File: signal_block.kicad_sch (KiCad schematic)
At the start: 9 parts, among them J6 Conn_01x04

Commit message: 24V Regulator, Pyro Igniter Circuit
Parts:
- renumbered J6 to J4
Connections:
- net SIGNAL_P: now reaches J4.2 (Pin_2), R14.2, R16.1, TC1.1 (+)
- net SIGNAL_N: now reaches J4.3 (Pin_3), R15.1, R17.1, TC1.2 (-)
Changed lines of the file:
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@@
+		)
+	)
+	(label "SIGNAL_N"
+		(at 125.73 93.98 0)
+		(effects
+			(font
+				(size 1.27 1.27)
+			)
+			(justify left bottom)
+		)
+	)
+	(label "SIGNAL_P"
+		(at 125.73 91.44 0)
+		(effects
+			(font
+				(size 1.27 1.27)
+			)
+			(justify left bottom)
 		)
 	)
@@
 		(in_pos_files yes)
 		(dnp no)
-		(property "Reference" "J6"
+		(property "Reference" "J4"
 			(at 116.84 83.058 0)
 			(show_name no)
@@
 			(project "mixed_signal_sensor_board"
 				(path "/5c142d60-6b5a-463f-88b9-a177eae7f51b/26b48b96-d6f0-4640-a594-6ae05ce5f71b"
+					(reference "J4")
+					(unit 1)
+				)
+				(path "/5c142d60-6b5a-463f-88b9-a177eae7f51b/3d2fab60-312f-4afa-9448-ea43b3519a6a"
+					(reference "J9")
+					(unit 1)
+				)
+				(path "/5c142d60-6b5a-463f-88b9-a177eae7f51b/83995c98-2fb2-4e6b-8c1a-49363bfa6bab"
+					(reference "J5")
+					(unit 1)
+				)
+				(path "/5c142d60-6b5a-463f-88b9-a177eae7f51b/8e376074-b16c-4624-98ef-c910278a89e5"
 					(reference "J6")
 					(unit 1)
 				)
-				(path "/5c142d60-6b5a-463f-88b9-a177eae7f51b/3d2fab60-312f-4afa-9448-ea43b3519a6a"
+				(path "/5c142d60-6b5a-463f-88b9-a177eae7f51b/a20a6c68-f4f4-4b40-90d6-d2c7554cb778"
 					(reference "J11")
 					(unit 1)
 				)
-				(path "/5c142d60-6b5a-463f-88b9-a177eae7f51b/83995c98-2fb2-4e6b-8c1a-49363bfa6bab"
+				(path "/5c142d60-6b5a-463f-88b9-a177eae7f51b/b2385cce-9f51-4d63-9d92-5a2772ad4011"
 					(reference "J7")
 					(unit 1)
 				)
-				(path "/5c142d60-6b5a-463f-88b9-a177eae7f51b/8e376074-b16c-4624-98ef-c910278a89e5"
+				(path "/5c142d60-6b5a-463f-88b9-a177eae7f51b/c788519d-2f00-4572-8a46-36c8c3e2499e"
 					(reference "J8")
 					(unit 1)
 				)
-				(path "/5c142d60-6b5a-463f-88b9-a177eae7f51b/a20a6c68-f4f4-4b40-90d6-d2c7554cb778"
-					(reference "J13")
-					(unit 1)
-				)
-				(path "/5c142d60-6b5a-463f-88b9-a177eae7f51b/b2385cce-9f51-4d63-9d92-5a2772ad4011"
-					(reference "J9")
-					(unit 1)
-				)
-				(path "/5c142d60-6b5a-463f-88b9-a177eae7f51b/c788519d-2f00-4572-8a46-36c8c3e2499e"
+				(path "/5c142d60-6b5a-463f-88b9-a177eae7f51b/fe701933-2939-43ec-a76b-ec9b5f6332a0"
 					(reference "J10")
-					(unit 1)
-				)
-				(path "/5c142d60-6b5a-463f-88b9-a177eae7f51b/fe701933-2939-43ec-a76b-ec9b5f6332a0"
-					(reference "J12")
 					(unit 1)
 				)
@@
 		(dnp no)
 		(fields_autoplaced yes)
-		(property "Reference" "#PWR059"
+		(property "Reference" "#PWR055"
 			(at 151.13 81.28 0)
 			(hide yes)
@@
 			(project "mixed_signal_sensor_board"
 				(path "/5c142d60-6b5a-463f-88b9-a177eae7f51b/26b48b96-d6f0-4640-a594-6ae05ce5f71b"
-					(reference "#PWR059")
+					(reference "#PWR055")
 					(unit 1)
 				)
 				(path "/5c142d60-6b5a-463f-88b9-a177eae7f51b/3d2fab60-312f-4afa-9448-ea43b3519a6a"
-					(reference "#PWR084")
+					(reference "#PWR080")
 					(unit 1)
 				)
 				(path "/5c142d60-6b5a-463f-88b9-a177eae7f51b/83995c98-2fb2-4e6b-8c1a-49363bfa6bab"
-					(reference "#PWR064")
+					(reference "#PWR060")
 					(unit 1)
 				)
 				(path "/5c142d60-6b5a-463f-88b9-a177eae7f51b/8e376074-b16c-4624-98ef-c910278a89e5"
-					(reference "#PWR069")
+					(reference "#PWR065")
 					(unit 1)
 				)
 				(path "/5c142d60-6b5a-463f-88b9-a177eae7f51b/a20a6c68-f4f4-4b40-90d6-d2c7554cb778"
-					(reference "#PWR094")
+					(reference "#PWR090")
 					(unit 1)
 				)
 				(path "/5c142d60-6b5a-463f-88b9-a177eae7f51b/b2385cce-9f51-4d63-9d92-5a2772ad4011"
-					(reference "#PWR074")
+					(reference "#PWR070")
 					(unit 1)
 				)
 				(path "/5c142d60-6b5a-463f-88b9-a177eae7f51b/c788519d-2f00-4572-8a46-36c8c3e2499e"
-					(reference "#PWR079")
+					(reference "#PWR075")
 					(unit 1)
 				)
 				(path "/5c142d60-6b5a-463f-88b9-a177eae7f51b/fe701933-2939-43ec-a76b-ec9b5f6332a0"
-					(reference "#PWR089")
+					(reference "#PWR085")
 					(unit 1)
 				)
@@
 		(dnp no)
 		(fields_autoplaced yes)
-		(property "Reference" "#PWR058"
+		(property "Reference" "#PWR054"
 			(at 120.65 96.52 0)
 			(hide yes)
@@
 			(project "mixed_signal_sensor_board"
 				(path "/5c142d60-6b5a-463f-88b9-a177eae7f51b/26b48b96-d6f0-4640-a594-6ae05ce5f71b"
-					(reference "#PWR058")
+					(reference "#PWR054")
 					(unit 1)
 				)
 				(path "/5c142d60-6b5a-463f-88b9-a177eae7f51b/3d2fab60-312f-4afa-9448-ea43b3519a6a"
-					(reference "#PWR083")
+					(reference "#PWR079")
 					(unit 1)
 				)
 				(path "/5c142d60-6b5a-463f-88b9-a177eae7f51b/83995c98-2fb2-4e6b-8c1a-49363bfa6bab"
-					(reference "#PWR063")
+					(reference "#PWR059")
 					(unit 1)
 				)
 				(path "/5c142d60-6b5a-463f-88b9-a177eae7f51b/8e376074-b16c-4624-98ef-c910278a89e5"
-					(reference "#PWR068")
+					(reference "#PWR064")
 					(unit 1)
 				)
 				(path "/5c142d60-6b5a-463f-88b9-a177eae7f51b/a20a6c68-f4f4-4b40-90d6-d2c7554cb778"
-					(reference "#PWR093")
+					(reference "#PWR089")
 					(unit 1)
 				)
 				(path "/5c142d60-6b5a-463f-88b9-a177eae7f51b/b2385cce-9f51-4d63-9d92-5a2772ad4011"
-					(reference "#PWR073")
+					(reference "#PWR069")
 					(unit 1)
 				)
 				(path "/5c142d60-6b5a-463f-88b9-a177eae7f51b/c788519d-2f00-4572-8a46-36c8c3e2499e"
-					(reference "#PWR078")
+					(reference "#PWR074")
 					(unit 1)
 				)
 				(path "/5c142d60-6b5a-463f-88b9-a177eae7f51b/fe701933-2939-43ec-a76b-ec9b5f6332a0"
-					(reference "#PWR088")
+					(reference "#PWR084")
 					(unit 1)
 				)
@@
 		(dnp no)
 		(fields_autoplaced yes)
-		(property "Reference" "#PWR060"
+		(property "Reference" "#PWR056"
 			(at 151.13 114.3 0)
 			(hide yes)
@@
 			(project "mixed_signal_sensor_board"
 				(path "/5c142d60-6b5a-463f-88b9-a177eae7f51b/26b48b96-d6f0-4640-a594-6ae05ce5f71b"
-					(reference "#PWR060")
+					(reference "#PWR056")
 					(unit 1)
 				)
 				(path "/5c142d60-6b5a-463f-88b9-a177eae7f51b/3d2fab60-312f-4afa-9448-ea43b3519a6a"
-					(reference "#PWR085")
+					(reference "#PWR081")
 					(unit 1)
 				)
 				(path "/5c142d60-6b5a-463f-88b9-a177eae7f51b/83995c98-2fb2-4e6b-8c1a-49363bfa6bab"
-					(reference "#PWR065")
+					(reference "#PWR061")
 					(unit 1)
 				)
 				(path "/5c142d60-6b5a-463f-88b9-a177eae7f51b/8e376074-b16c-4624-98ef-c910278a89e5"
-					(reference "#PWR070")
+					(reference "#PWR066")
 					(unit 1)
 				)
 				(path "/5c142d60-6b5a-463f-88b9-a177eae7f51b/a20a6c68-f4f4-4b40-90d6-d2c7554cb778"
-					(reference "#PWR095")
+					(reference "#PWR091")
 					(unit 1)
 				)
 				(path "/5c142d60-6b5a-463f-88b9-a177eae7f51b/b2385cce-9f51-4d63-9d92-5a2772ad4011"
-					(reference "#PWR075")
+					(reference "#PWR071")
 					(unit 1)
 				)
 				(path "/5c142d60-6b5a-463f-88b9-a177eae7f51b/c788519d-2f00-4572-8a46-36c8c3e2499e"
-					(reference "#PWR080")
+					(reference "#PWR076")
 					(unit 1)
 				)
 				(path "/5c142d60-6b5a-463f-88b9-a177eae7f51b/fe701933-2939-43ec-a76b-ec9b5f6332a0"
-					(reference "#PWR090")
+					(reference "#PWR086")
 					(unit 1)
 				)
@@
 		(dnp no)
 		(fields_autoplaced yes)
-		(property "Reference" "#PWR057"
+		(property "Reference" "#PWR053"
 			(at 120.65 88.9 0)
 			(hide yes)
@@
 			(project "mixed_signal_sensor_board"
 				(path "/5c142d60-6b5a-463f-88b9-a177eae7f51b/26b48b96-d6f0-4640-a594-6ae05ce5f71b"
-					(reference "#PWR057")
+					(reference "#PWR053")
 					(unit 1)
 				)
 				(path "/5c142d60-6b5a-463f-88b9-a177eae7f51b/3d2fab60-312f-4afa-9448-ea43b3519a6a"
-					(reference "#PWR082")
+					(reference "#PWR078")
 					(unit 1)
 				)
 				(path "/5c142d60-6b5a-463f-88b9-a177eae7f51b/83995c98-2fb2-4e6b-8c1a-49363bfa6bab"
-					(reference "#PWR062")
+					(reference "#PWR058")
 					(unit 1)
 				)
 				(path "/5c142d60-6b5a-463f-88b9-a177eae7f51b/8e376074-b16c-4624-98ef-c910278a89e5"
-					(reference "#PWR067")
+					(reference "#PWR063")
 					(unit 1)
 				)
 				(path "/5c142d60-6b5a-463f-88b9-a177eae7f51b/a20a6c68-f4f4-4b40-90d6-d2c7554cb778"
-					(reference "#PWR092")
+					(reference "#PWR088")
 					(unit 1)
 				)
 				(path "/5c142d60-6b5a-463f-88b9-a177eae7f51b/b2385cce-9f51-4d63-9d92-5a2772ad4011"
-					(reference "#PWR072")
+					(reference "#PWR068")
 					(unit 1)
 				)
 				(path "/5c142d60-6b5a-463f-88b9-a177eae7f51b/c788519d-2f00-4572-8a46-36c8c3e2499e"
-					(reference "#PWR077")
+					(reference "#PWR073")
 					(unit 1)
 				)
 				(path "/5c142d60-6b5a-463f-88b9-a177eae7f51b/fe701933-2939-43ec-a76b-ec9b5f6332a0"
-					(reference "#PWR087")
+					(reference "#PWR083")
 					(unit 1)
 				)
@@
 		(dnp no)
 		(fields_autoplaced yes)
-		(property "Reference" "#PWR061"
+		(property "Reference" "#PWR057"
 			(at 193.04 92.71 0)
 			(hide yes)
@@
 			(project "mixed_signal_sensor_board"
 				(path "/5c142d60-6b5a-463f-88b9-a177eae7f51b/26b48b96-d6f0-4640-a594-6ae05ce5f71b"
-					(reference "#PWR061")
+					(reference "#PWR057")
 					(unit 1)
 				)
 				(path "/5c142d60-6b5a-463f-88b9-a177eae7f51b/3d2fab60-312f-4afa-9448-ea43b3519a6a"
-					(reference "#PWR086")
+					(reference "#PWR082")
 					(unit 1)
 				)
 				(path "/5c142d60-6b5a-463f-88b9-a177eae7f51b/83995c98-2fb2-4e6b-8c1a-49363bfa6bab"
-					(reference "#PWR066")
+					(reference "#PWR062")
 					(unit 1)
 				)
 				(path "/5c142d60-6b5a-463f-88b9-a177eae7f51b/8e376074-b16c-4624-98ef-c910278a89e5"
-					(reference "#PWR071")
+					(reference "#PWR067")
 					(unit 1)
 				)
 				(path "/5c142d60-6b5a-463f-88b9-a177eae7f51b/a20a6c68-f4f4-4b40-90d6-d2c7554cb778"
-					(reference "#PWR096")
+					(reference "#PWR092")
 					(unit 1)
 				)
 				(path "/5c142d60-6b5a-463f-88b9-a177eae7f51b/b2385cce-9f51-4d63-9d92-5a2772ad4011"
-					(reference "#PWR076")
+					(reference "#PWR072")
 					(unit 1)
 				)
 				(path "/5c142d60-6b5a-463f-88b9-a177eae7f51b/c788519d-2f00-4572-8a46-36c8c3e2499e"
-					(reference "#PWR081")
+					(reference "#PWR077")
 					(unit 1)
 				)
 				(path "/5c142d60-6b5a-463f-88b9-a177eae7f51b/fe701933-2939-43ec-a76b-ec9b5f6332a0"
-					(reference "#PWR091")
-					(unit 1)
-				)
+					(reference "#PWR087")
+					(unit 1)
+				)

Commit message: Pyro fault detection, Decoupling Caps STM32, Initial PCB Layout
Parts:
- renumbered C23 to C29, C24 to C30, C25 to C31
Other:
- moved on the sheet: C29, C30, C31, J4, R14, R15, R16, R17, TC1

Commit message: Step files, SMD connectors, reduced size
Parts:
- J4: footprint Connector_JST:JST_XH_S4B-XH-A_1x04_P2.50mm_Horizontal -> Connector_JST:JST_PH_S4B-PH-SM4-TB_1x04-1MP_P2.00mm_Horizontal
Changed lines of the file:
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@@
 			)
 		)
-		(property "Footprint" "Connector_JST:JST_XH_S4B-XH-A_1x04_P2.50mm_Horizontal"
+		(property "Footprint" "Connector_JST:JST_PH_S4B-PH-SM4-TB_1x04-1MP_P2.00mm_Horizontal"
 			(at 110.49 97.79 0)
 			(hide yes)

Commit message: replaced signal blocks, shortening board, adding precise positioning
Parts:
- renumbered J4 to J5, R14 to R15, R15 to R16, R16 to R17, R17 to R18

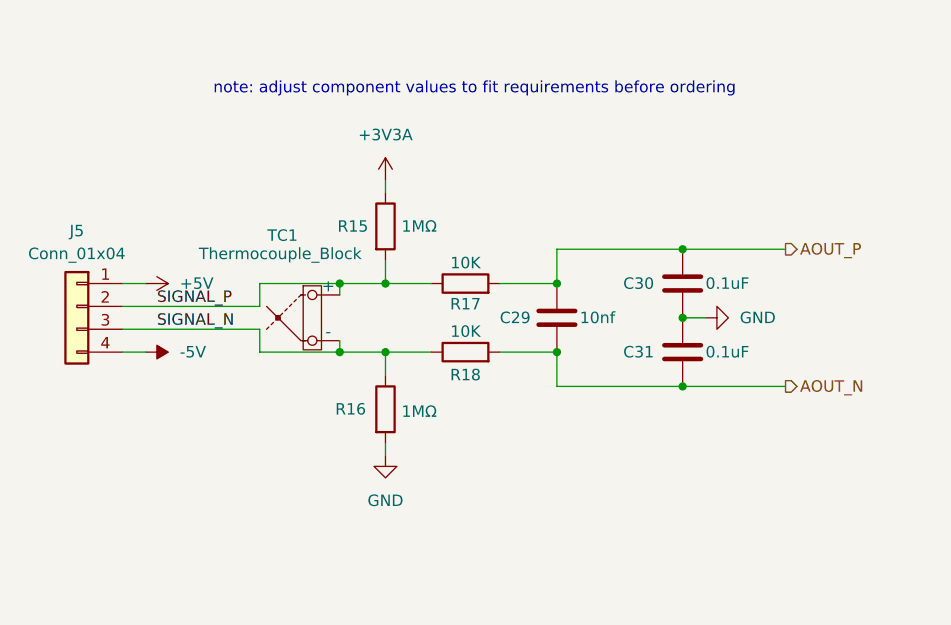
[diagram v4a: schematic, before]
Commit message: PYRO done, schematic structure/convention update, pyro and reverse polarity components selected
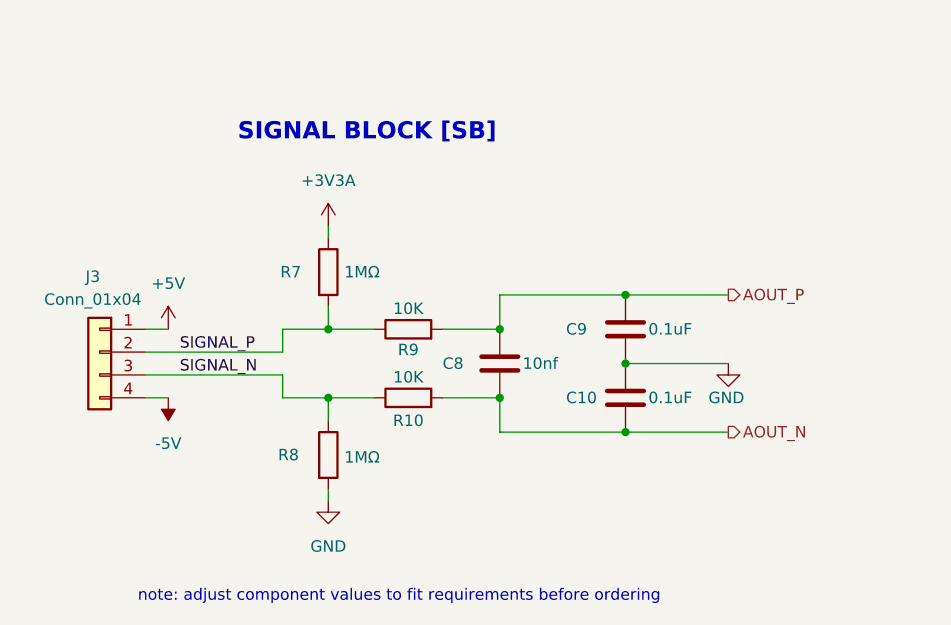
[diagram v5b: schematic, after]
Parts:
- removed TC1: Thermocouple_Block, symbol Device:Thermocouple_Block
- renumbered C31 to C10, C29 to C8, C30 to C9, J5 to J3, R18 to R10, R15 to R7, R16 to R8, R17 to R9
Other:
- note added: "SIGNAL BLOCK [SB]"
- moved on the sheet: C10, C8, C9, J3, R10, R7, R8, R9
